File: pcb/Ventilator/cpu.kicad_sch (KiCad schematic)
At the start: 22 parts, among them J1 Conn_02x03_Top_Bottom, SW1 Reset, U1 W25Q128JVS, U2 RP2040

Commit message: - all parts connected, placed partially
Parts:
- added H1: WIZ850IO, W5500:WIZ850IO, symbol W5500:WIZ850IO
- added R4: 10k, Resistor_SMD:R_0805_2012Metric, symbol Device:R
- J1: footprint (none) -> Connector_PinHeader_2.54mm:PinHeader_2x03_P2.54mm_Vertical
- R1, R2: footprint (none) -> Resistor_SMD:R_0805_2012Metric
- XTAL1: footprint XTAL_ABLS_ABR -> Xtal:ABLS-12.000MHZ-B4-T
- renumbered C2 to C1, C11 to C10, C12 to C11, C13 to C12, C14 to C13, C3 to C2, C4 to C3, C5 to C4, C6 to C5, C7 to C6, C8 to C7, C9 to C8, C10 to C9
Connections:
- net +3.3V: now also J1.5 (Pin_5), H1.8 (3.3V_1), H1.9 (3.3V_2), R4.2
- net GND: now also J1.1 (Pin_1), H1.1 (GND_1), H1.2 (GND_2), H1.7 (GND_3)
- net SWCLK: now reaches J1.2 (Pin_2)
- net SWCLK: now also U2.24 (SWCLK)
- net RX: now reaches J1.4 (Pin_4)
- net RX: now also U2.3 (GPIO1)
- net SWD: now reaches J1.6 (Pin_6)
- net SWD: now also U2.25 (SWD)
- net MISO: now reaches U2.27 (GPIO16)
- net MISO: now also H1.12 (MISO)
- net SCNN: now reaches U2.28 (GPIO17)
- net SCNN: now also H1.5 (SCNN)
- net SCLK: now reaches U2.29 (GPIO18)
- net SCLK: now also H1.4 (SCLK)
- net MOSI: now reaches U2.30 (GPIO19)
- net MOSI: now also H1.3 (MOSI)
- net RSTN: now reaches U2.31 (GPIO20)
- net RSTN: now also H1.11 (RSTN), R4.1
- no-connect marks 22 -> 20

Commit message: - voor omschakeling naar rp pico
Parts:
- removed C10: 100n, Capacitor_SMD:C_1206_3216Metric_Pad1.33x1.80mm_HandSolder, symbol Device:C
- C10: renamed from C11; footprint Capacitor_SMD:C_1206_3216Metric_Pad1.33x1.80mm_HandSolder -> Capacitor_SMD:C_0805_2012Metric_Pad1.18x1.45mm_HandSolder
- C11: renamed from C12; footprint Capacitor_SMD:C_1206_3216Metric_Pad1.33x1.80mm_HandSolder -> Capacitor_SMD:C_0805_2012Metric_Pad1.18x1.45mm_HandSolder
- C12: renamed from C13; footprint Capacitor_SMD:C_1206_3216Metric_Pad1.33x1.80mm_HandSolder -> Capacitor_SMD:C_0805_2012Metric_Pad1.18x1.45mm_HandSolder
- C3, C4, C5, C6, C7, C8, C9: footprint Capacitor_SMD:C_1206_3216Metric_Pad1.33x1.80mm_HandSolder -> Capacitor_SMD:C_0805_2012Metric_Pad1.18x1.45mm_HandSolder
- R2: value 1k -> 10k
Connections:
- net +1V1: now reaches C3.1, C4.2, C5.2, U2.23 (DVDD), U2.45 (VREG_VOUT), U2.50 (DVDD)

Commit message: - voor autorouter
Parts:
- removed C1, C2: 22p, Capacitor_SMD:C_1206_3216Metric_Pad1.33x1.80mm_HandSolder, symbol Device:C
- removed C10, C11, C12, C4, C5, C7, C8, C9: 100n, Capacitor_SMD:C_0805_2012Metric_Pad1.18x1.45mm_HandSolder, symbol Device:C
- removed C3, C6: 1u, Capacitor_SMD:C_0805_2012Metric_Pad1.18x1.45mm_HandSolder, symbol Device:C
- removed R1: 1k, Resistor_SMD:R_0805_2012Metric, symbol Device:R
- removed U1: W25Q128JVS, Package_SO:SOIC-8_5.23x5.23mm_P1.27mm, symbol Memory_Flash:W25Q128JVS
- removed U2: RP2040, Package_DFN_QFN:QFN-56-1EP_7x7mm_P0.4mm_EP3.2x3.2mm, symbol MCU_RaspberryPi:RP2040
- removed XTAL1: ABLS-12.000MHZ-B4-T, Xtal:ABLS-12.000MHZ-B4-T, symbol XTal:ABLS-12.000MHZ-B4-T
- added JP1: SolderJumper_3_Bridged12, Jumper:SolderJumper-3_P1.3mm_Bridged12_Pad1.0x1.5mm, symbol Jumper:SolderJumper_3_Bridged12
- added U1: Pico, MCU_RaspberryPi_and_Boards:RPi_Pico_SMD_TH, symbol MCU_RaspberryPi_and_Boards:Pico
- renumbered R3 to R1, R4 to R2, R2 to R3
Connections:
- net VCC is gone; now on net +3.3V: R1.2
- net +3.3V: now also U1.36 (3V3)
- net GND: now also U1.13 (GND), U1.18 (GND), U1.23 (GND), U1.28 (GND), U1.3 (GND), U1.33 (AGND), U1.38 (GND), U1.42 (GND), U1.8 (GND)
- net IN1: now also U1.5 (GPIO3)
- net IN2: now also U1.6 (GPIO4)
- net IN3: now also U1.7 (GPIO5)
- net IN4: now also U1.9 (GPIO6)
- net MISO: now also U1.21 (GPIO16)
- net MOSI: now also U1.25 (GPIO19)
- net OUT1: now also U1.10 (GPIO7)
- net OUT2: now also U1.19 (GPIO14)
- net OUT3: now also U1.20 (GPIO15)
- net RSTN: now also U1.26 (GPIO20)
- net RX: now also JP1.2 (C)
- net SCLK: now also U1.24 (GPIO18)
- net SCNN: now also U1.22 (GPIO17)
- net SWCLK: now also U1.41 (SWCLK)
- net SWD: now also U1.43 (SWDIO)
- net at R3.1, SW1.2: now also U1.30 (RUN)
- net at D1.1 (K): now also U1.4 (GPIO2)
- new net: JP1.1 (A), U1.2 (GPIO1)
- new net: JP1.3 (B), U1.1 (GPIO0)
- new net +5V: U1.39 (VSYS)
- no-connect marks 20 -> 14
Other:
- moved on the sheet: D1, H1, R1, R2, R3, SW1

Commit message: - as ordered (30/12/2022)
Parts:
- added JP1: SolderJumper_2_Open, symbol Jumper:SolderJumper_2_Open
- renumbered JP1 to JP2
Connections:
- net +3.3V: now also JP1.2 (B); no longer J1.5 (Pin_5)
- new net: J1.5 (Pin_5), JP1.1 (A)
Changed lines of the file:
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@@
+    (stroke (width 0) (type default) (color 0 0 0 0))
+  )
+  (wire (pts (xy 92.71 152.4) (xy 92.71 154.94))
     (stroke (width 0) (type default) (color 0 0 0 0))
   )
@@
     (stroke (width 0) (type default) (color 0 0 0 0))
   )
+  (wire (pts (xy 97.79 95.25) (xy 118.11 95.25))
+    (stroke (width 0) (type default) (color 0 0 0 0))
+  )
+  (wire (pts (xy 165.1 133.35) (xy 165.1 135.89))
+    (stroke (width 0) (type default) (color 0 0 0 0))
+  )
+  (wire (pts (xy 76.2 157.48) (xy 82.55 157.48))
+    (stroke (width 0) (type default) (color 0 0 0 0))
+  )
+  (wire (pts (xy 109.22 67.31) (xy 118.11 67.31))
+    (stroke (width 0) (type default) (color 0 0 0 0))
+  )
+  (wire (pts (xy 152.4 147.32) (xy 161.29 147.32))
+    (stroke (width 0) (type default) (color 0 0 0 0))
+  )
+  (wire (pts (xy 175.26 73.66) (xy 175.26 74.93))
+    (stroke (width 0) (type default) (color 0 0 0 0))
+  )
+  (wire (pts (xy 109.22 54.61) (xy 118.11 54.61))
+    (stroke (width 0) (type default) (color 0 0 0 0))
+  )
+  (wire (pts (xy 153.67 59.69) (xy 158.75 59.69))
+    (stroke (width 0) (type default) (color 0 0 0 0))
+  )
   (wire (pts (xy 76.2 154.94) (xy 85.09 154.94))
     (stroke (width 0) (type default) (color 0 0 0 0))
   )
-  (wire (pts (xy 97.79 95.25) (xy 118.11 95.25))
-    (stroke (width 0) (type default) (color 0 0 0 0))
-  )
-  (wire (pts (xy 165.1 133.35) (xy 165.1 135.89))
-    (stroke (width 0) (type default) (color 0 0 0 0))
-  )
-  (wire (pts (xy 76.2 157.48) (xy 82.55 157.48))
-    (stroke (width 0) (type default) (color 0 0 0 0))
-  )
-  (wire (pts (xy 109.22 67.31) (xy 118.11 67.31))
-    (stroke (width 0) (type default) (color 0 0 0 0))
-  )
-  (wire (pts (xy 152.4 147.32) (xy 161.29 147.32))
-    (stroke (width 0) (type default) (color 0 0 0 0))
-  )
-  (wire (pts (xy 175.26 73.66) (xy 175.26 74.93))
-    (stroke (width 0) (type default) (color 0 0 0 0))
-  )
-  (wire (pts (xy 109.22 54.61) (xy 118.11 54.61))
-    (stroke (width 0) (type default) (color 0 0 0 0))
-  )
-  (wire (pts (xy 153.67 59.69) (xy 158.75 59.69))
-    (stroke (width 0) (type default) (color 0 0 0 0))
-  )
   (wire (pts (xy 161.29 133.35) (xy 165.1 133.35))
-    (stroke (width 0) (type default) (color 0 0 0 0))
-  )
-  (wire (pts (xy 85.09 154.94) (xy 85.09 153.67))
     (stroke (width 0) (type default) (color 0 0 0 0))
   )
@@
     )
     (pin "1")
+  )
+  (symbol (lib_id "Jumper:SolderJumper_2_Open") (at 88.9 154.94 0) (unit 1)
+    (in_bom yes) (on_board yes) (fields_autoplaced)
+    (property "Reference" "JP1" (id 0) (at 88.9 151.13 0))
+    (property "Value" "SolderJumper_2_Open" (id 1) (at 88.9 151.13 0)
+      (effects (font (size 1.27 1.27)) hide)
+    )
+    (property "Footprint" "" (id 2) (at 88.9 154.94 0)
+      (effects (font (size 1.27 1.27)) hide)
+    )
+    (property "Datasheet" "~" (id 3) (at 88.9 154.94 0)
+      (effects (font (size 1.27 1.27)) hide)
+    )
+    (pin "1")
+    (pin "2")
   )
   (symbol (lib_id "Connector_Generic:Conn_02x03_Top_Bottom") (at 68.58 154.94 0) (unit 1)
@@
   (symbol (lib_id "Jumper:SolderJumper_3_Bridged12") (at 113.03 44.45 0) (mirror x) (unit 1)
     (in_bom yes) (on_board yes) (fields_autoplaced)
-    (property "Reference" "JP1" (id 0) (at 113.03 48.26 0))
+    (property "Reference" "JP2" (id 0) (at 113.03 48.26 0))
     (property "Value" "SolderJumper_3_Bridged12" (id 1) (at 113.03 50.8 0)
       (effects (font (size 1.27 1.27)) hide)
@@
     (pin "1")
   )
-  (symbol (lib_id "power:+3.3V") (at 85.09 153.67 0) (unit 1)
-    (in_bom yes) (on_board yes) (fields_autoplaced)
-    (property "Reference" "#PWR02" (id 0) (at 85.09 157.48 0)
-      (effects (font (size 1.27 1.27)) hide)
-    )
-    (property "Value" "+3.3V" (id 1) (at 85.09 148.59 0))
-    (property "Footprint" "" (id 2) (at 85.09 153.67 0)
-      (effects (font (size 1.27 1.27)) hide)
-    )
-    (property "Datasheet" "" (id 3) (at 85.09 153.67 0)
+  (symbol (lib_id "power:+3.3V") (at 92.71 152.4 0) (unit 1)
+    (in_bom yes) (on_board yes) (fields_autoplaced)
+    (property "Reference" "#PWR02" (id 0) (at 92.71 156.21 0)
+      (effects (font (size 1.27 1.27)) hide)
+    )
+    (property "Value" "+3.3V" (id 1) (at 92.71 147.32 0))
+    (property "Footprint" "" (id 2) (at 92.71 152.4 0)
+      (effects (font (size 1.27 1.27)) hide)
+    )
+    (property "Datasheet" "" (id 3) (at 92.71 152.4 0)
       (effects (font (size 1.27 1.27)) hide)
     )
@@
   (symbol (lib_id "power:GND") (at 107.95 81.28 0) (unit 1)
     (in_bom yes) (on_board yes) (fields_autoplaced)
-    (property "Reference" "#PWR04" (id 0) (at 107.95 87.63 0)
+    (property "Reference" "#PWR05" (id 0) (at 107.95 87.63 0)
       (effects (font (size 1.27 1.27)) hide)
     )
@@
   (symbol (lib_id "power:GND") (at 105.41 92.71 270) (unit 1)
     (in_bom yes) (on_board yes) (fields_autoplaced)
-    (property "Reference" "#PWR05" (id 0) (at 99.06 92.71 0)
-      (effects (font (size 1.27 1.27)) hide)
-    )
+    (property "Reference" "#PWR04" (id 0) (at 99.06 92.71 0)
+      (effects (font (size 1.27 1.27)) hide)
+    )

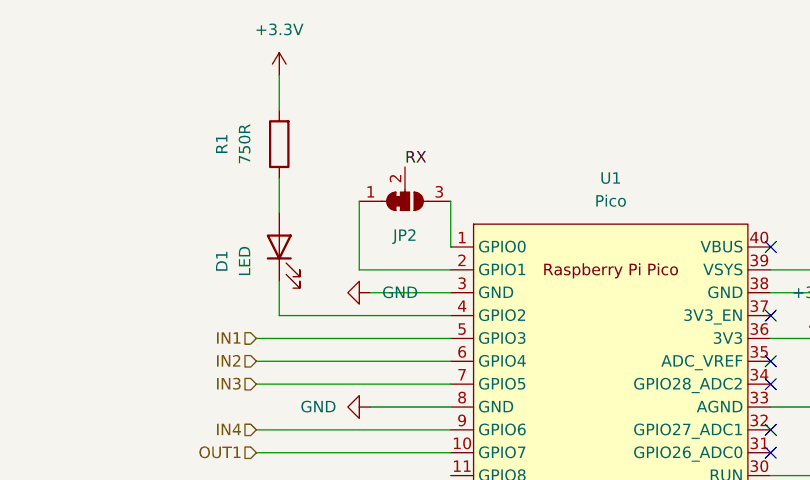
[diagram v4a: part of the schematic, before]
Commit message: -Ventcontrol 1.2 (routed)
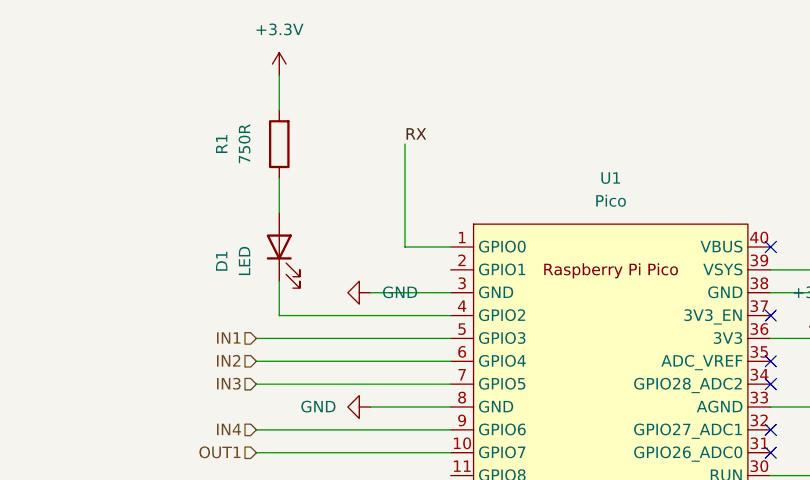
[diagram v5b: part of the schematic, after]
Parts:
- removed JP2: SolderJumper_3_Bridged12, Jumper:SolderJumper-3_P1.3mm_Bridged12_Pad1.0x1.5mm, symbol Jumper:SolderJumper_3_Bridged12
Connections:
- net RX: now also U1.1 (GPIO0)
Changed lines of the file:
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@@
+    (stroke (width 0) (type default) (color 0 0 0 0))
+  )
+  (wire (pts (xy 113.03 49.53) (xy 118.11 49.53))
     (stroke (width 0) (type default) (color 0 0 0 0))
   )
@@
     (stroke (width 0) (type default) (color 0 0 0 0))
   )
-  (wire (pts (xy 107.95 44.45) (xy 107.95 52.07))
-    (stroke (width 0) (type default) (color 0 0 0 0))
-  )
   (wire (pts (xy 152.4 144.78) (xy 165.1 144.78))
     (stroke (width 0) (type default) (color 0 0 0 0))
@@
     (stroke (width 0) (type default) (color 0 0 0 0))
   )
-  (wire (pts (xy 107.95 52.07) (xy 118.11 52.07))
-    (stroke (width 0) (type default) (color 0 0 0 0))
-  )
   (wire (pts (xy 110.49 134.62) (xy 110.49 137.16))
     (stroke (width 0) (type default) (color 0 0 0 0))
@@
     (stroke (width 0) (type default) (color 0 0 0 0))
   )
-  (wire (pts (xy 118.11 44.45) (xy 118.11 49.53))
-    (stroke (width 0) (type default) (color 0 0 0 0))
-  )
   (wire (pts (xy 99.06 53.34) (xy 99.06 57.15))
     (stroke (width 0) (type default) (color 0 0 0 0))
@@
     (stroke (width 0) (type default) (color 0 0 0 0))
   )
+  (wire (pts (xy 113.03 38.1) (xy 113.03 49.53))
+    (stroke (width 0) (type default) (color 0 0 0 0))
+  )
   (wire (pts (xy 163.83 80.01) (xy 163.83 81.28))
     (stroke (width 0) (type default) (color 0 0 0 0))
@@
     (effects (font (size 1.27 1.27)) (justify left bottom))
   )
-  (label "RX" (at 113.03 40.64 0)
+  (label "RX" (at 113.03 38.1 0)
     (effects (font (size 1.27 1.27)) (justify left bottom))
   )
@@
     (pin "1")
   )
-  (symbol (lib_id "Jumper:SolderJumper_3_Bridged12") (at 113.03 44.45 0) (mirror x) (unit 1)
-    (in_bom yes) (on_board yes) (fields_autoplaced)
-    (property "Reference" "JP2" (id 0) (at 113.03 48.26 0))
-    (property "Value" "SolderJumper_3_Bridged12" (id 1) (at 113.03 50.8 0)
-      (effects (font (size 1.27 1.27)) hide)
-    )
-    (property "Footprint" "Jumper:SolderJumper-3_P1.3mm_Bridged12_Pad1.0x1.5mm" (id 2) (at 113.03 44.45 0)
-      (effects (font (size 1.27 1.27)) hide)
-    )
-    (property "Datasheet" "~" (id 3) (at 113.03 44.45 0)
-      (effects (font (size 1.27 1.27)) hide)
-    )
-    (pin "1")
-    (pin "2")
-    (pin "3")
-  )
   (symbol (lib_id "Device:R") (at 99.06 38.1 180) (unit 1)
